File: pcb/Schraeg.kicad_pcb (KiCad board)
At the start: 2 copper layers, 84.5 x 128.5 mm, 118 parts, among them J1 PJ398SM, J2 PJ398SM, J3 PJ398SM, J4 PJ398SM, J5 PJ398SM, J6 PJ398SM, J7 PJ398SM, J8 POWER, U1 TL074, U2 TL074, U3 V2164, U4 TL074, U5 TL074

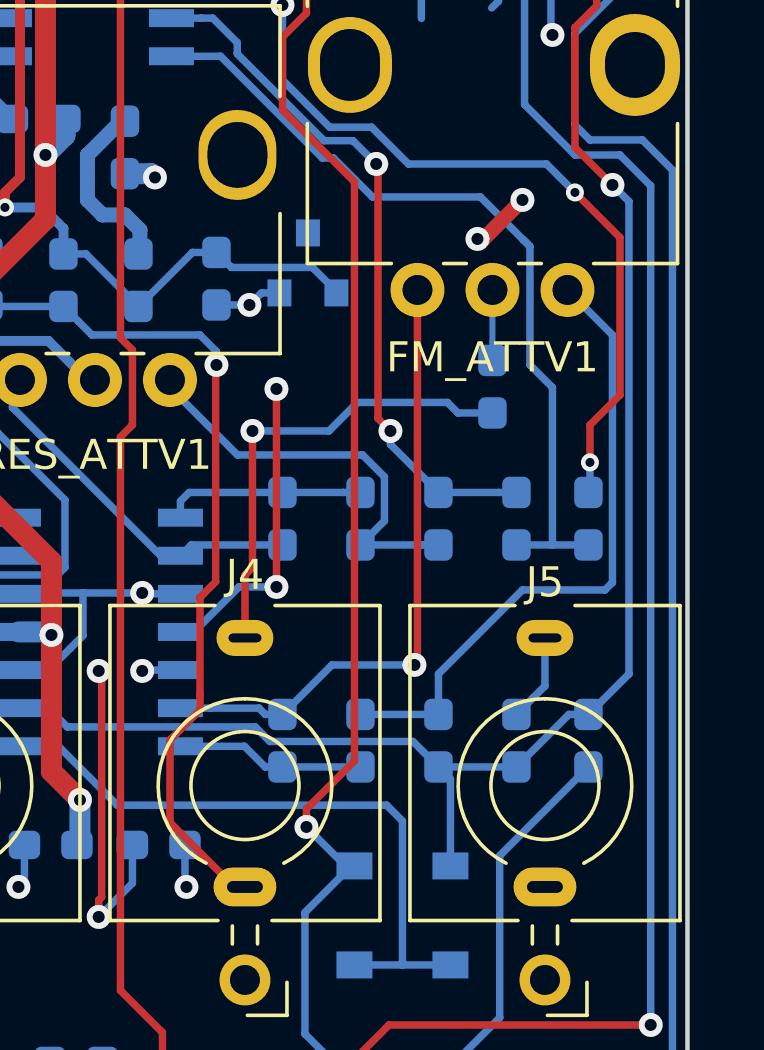
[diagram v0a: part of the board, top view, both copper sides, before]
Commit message: #1 - Corrected FM atennuverter
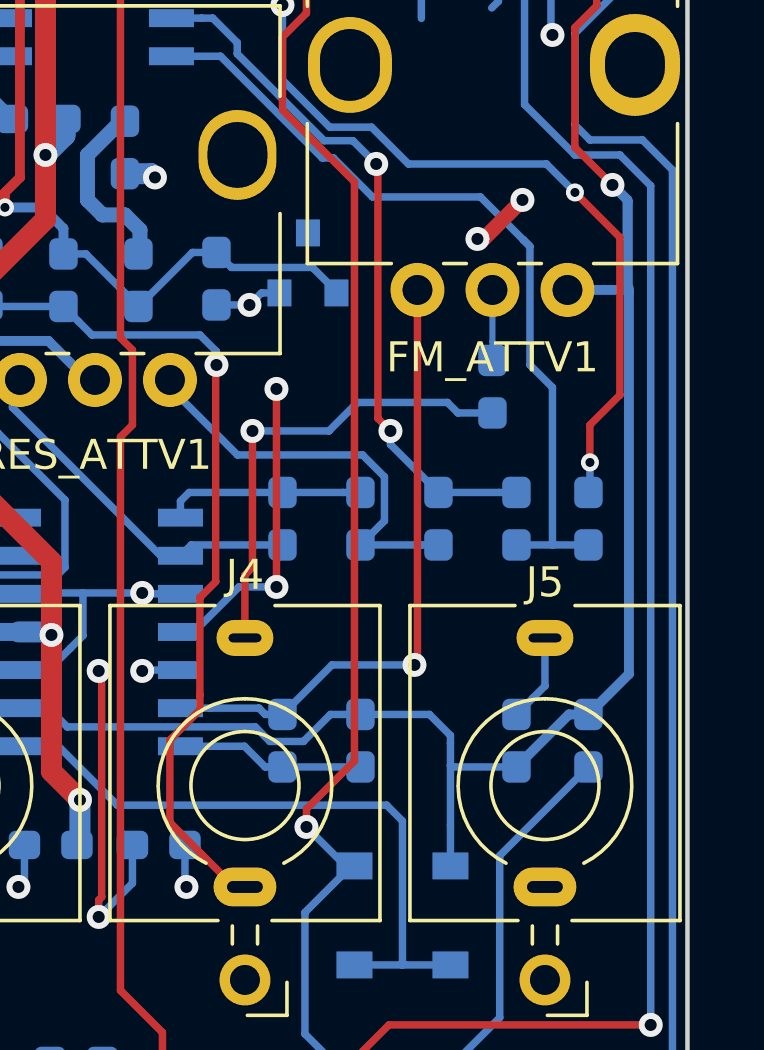
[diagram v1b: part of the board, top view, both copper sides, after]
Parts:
- removed R8: 100k, Resistor_SMD:R_0603_1608Metric_Pad1.05x0.95mm_HandSolder
- FM_ATTV1: value 100k -> 100KB
- R2, R5: value 100k -> 47K
- R48: value 100K -> 47K
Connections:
- FM_ATTV1 pad 1: Net-(FM_ATTV1-Pad1) -> Net-(D1-Pad2)
- R5 pad 1: Net-(FM_ATTV1-Pad1) -> Net-(D1-Pad2)
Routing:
- net Net-(FM_ATTV1-Pad1): track 21.4 -> 0.00 mm
- net Net-(D1-Pad2): track 80.6 -> 100.4 mm

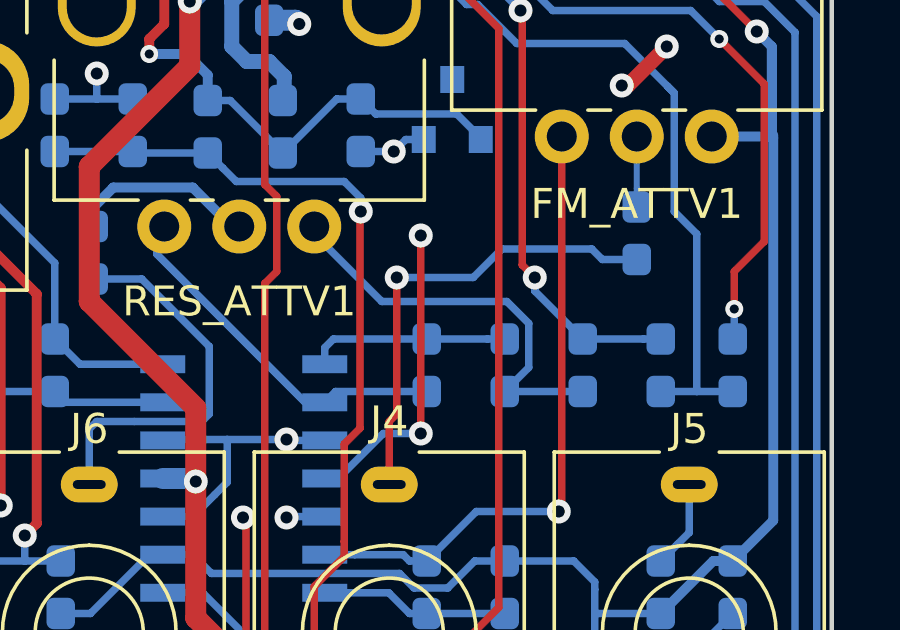
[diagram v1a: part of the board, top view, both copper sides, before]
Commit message: #2 - Corrected resonance attenuverter
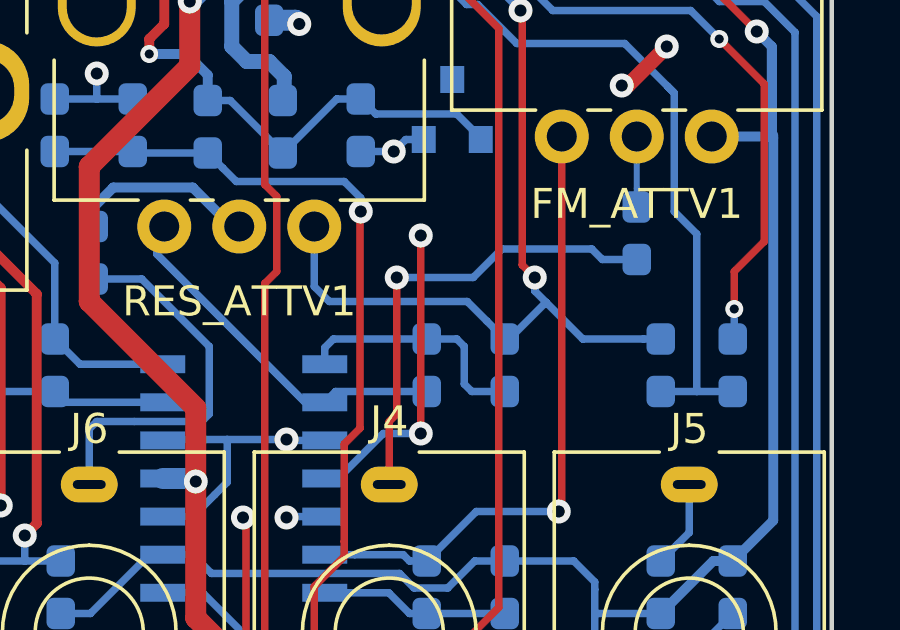
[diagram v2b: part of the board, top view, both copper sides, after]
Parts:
- removed R11: 100k, Resistor_SMD:R_0603_1608Metric_Pad1.05x0.95mm_HandSolder
- RES_ATTV1: value 100k -> 100KB
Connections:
- R13 pad 2: Net-(R11-Pad1) -> Net-(R13-Pad2)
- R6 pad 1: Net-(R11-Pad2) -> Net-(R3-Pad1)
- R6 pad 2: Net-(R3-Pad1) -> Net-(R13-Pad2)
- RES_ATTV1 pad 1: Net-(R11-Pad2) -> Net-(R13-Pad2)
- U2 pad 6: Net-(R11-Pad1) -> Net-(R13-Pad2)
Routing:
- net Net-(R13-Pad2): track 0.00 -> 34.4 mm, vias 0 -> 2
- net Net-(R11-Pad1): track 23.5 -> 0.00 mm, vias 2 -> 0
- net Net-(R11-Pad2): track 13.9 -> 0.00 mm
- net Net-(R3-Pad1): track 6.67 -> 8.13 mm

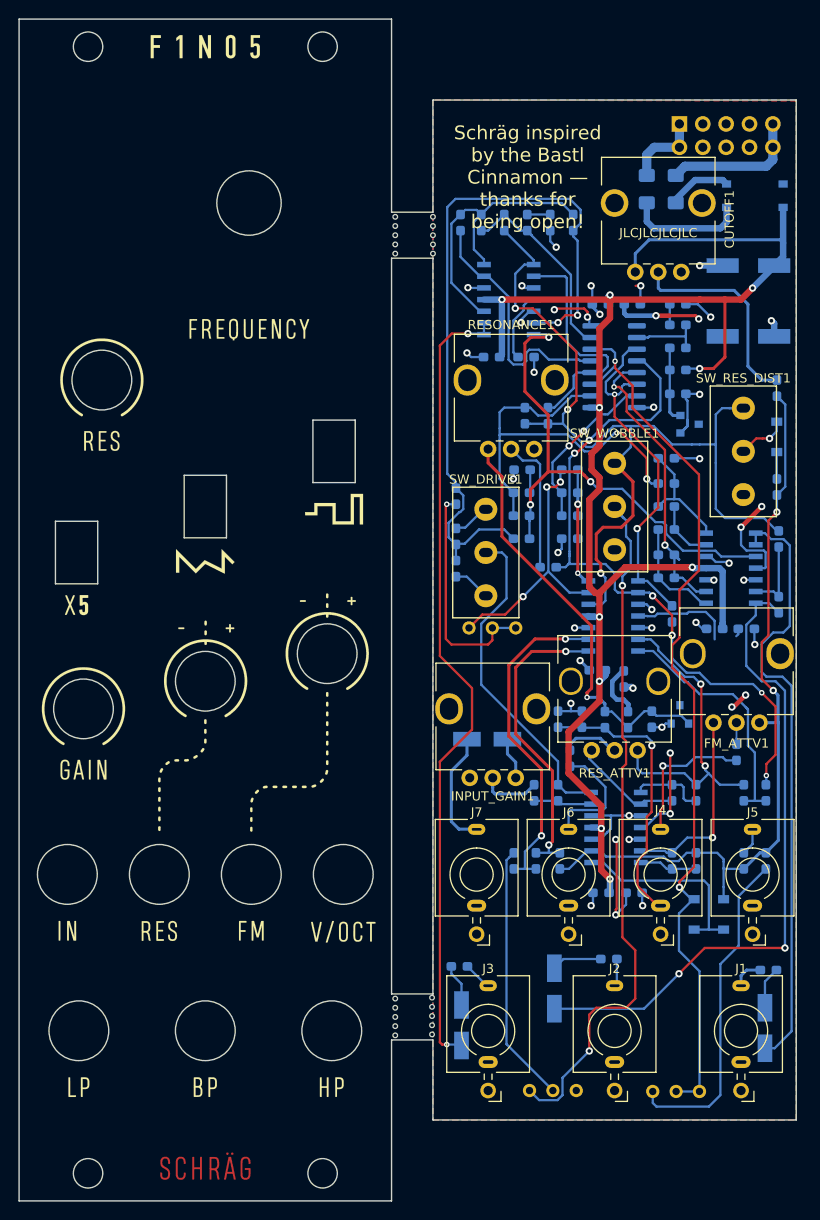
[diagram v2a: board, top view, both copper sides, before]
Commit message: Changed paths to use Kicad variables
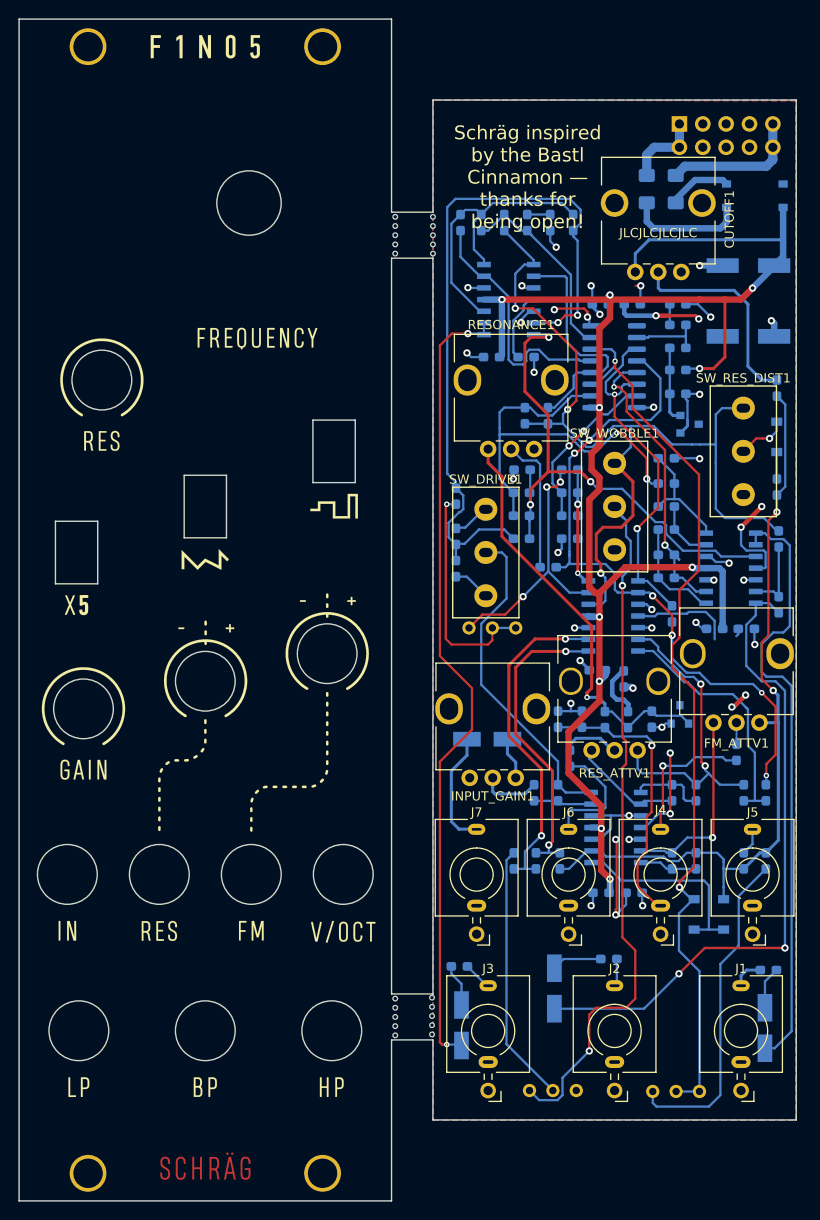
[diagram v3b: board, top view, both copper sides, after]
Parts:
- added REF**: MountingHole_3.2mm_M3, MountingHole:MountingHole_3.2mm_M3, F.Cu at (33.0, 125.5)
- added REF**: MountingHole_3.2mm_M3, MountingHole:MountingHole_3.2mm_M3, F.Cu at (7.50, 125.5)
- added REF**: MountingHole_3.2mm_M3, MountingHole:MountingHole_3.2mm_M3, F.Cu at (7.50, 3.00)
- added REF**: MountingHole_3.2mm_M3, MountingHole:MountingHole_3.2mm_M3, F.Cu at (33.0, 3.00)
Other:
- outline, holes or cut-outs redrawn
